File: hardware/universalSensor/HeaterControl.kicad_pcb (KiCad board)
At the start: 2 copper layers, 24.4 x 24.9 mm, 16 parts, among them J1 DS18B20, J4 Ext, P1 TC2030-CTX, SW1 BTN, U2 BL654, U3 SHT30-DIS-B

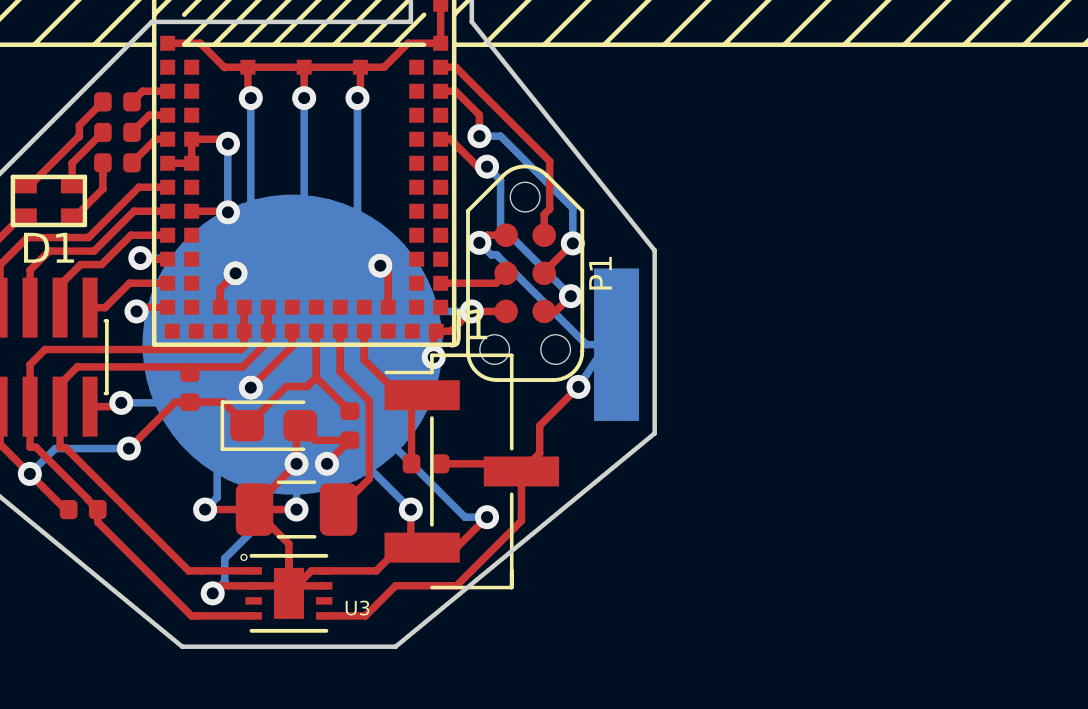
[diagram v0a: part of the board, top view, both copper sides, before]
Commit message: Add dev port do univeral board
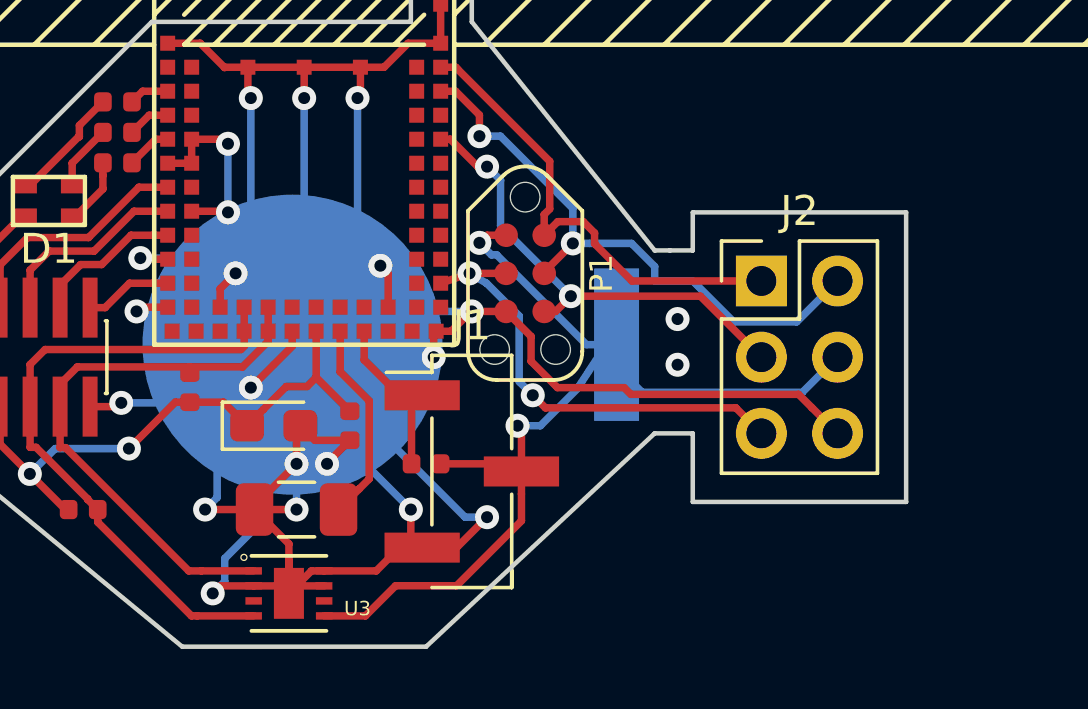
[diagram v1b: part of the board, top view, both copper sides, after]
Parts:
- added J2: DEV_PORT, Connector_PinHeader_2.54mm:PinHeader_2x03_P2.54mm_Vertical, F.Cu at (119.4, 86.4)
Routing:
- net GND: track 159.2 -> 172.5 mm
- net /nRESET: track 2.32 -> 15.4 mm, vias 0 -> 2
- net /SWDCLK_EXT: track 9.00 -> 19.8 mm
- net +3V3: track 50.3 -> 59.8 mm
- net /SWDIO_EXT: track 7.58 -> 16.8 mm, vias 0 -> 1
- net /SWO_EXT: track 8.50 -> 15.7 mm
- net (no net): vias 0 -> 2
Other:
- board size 24.4 x 24.9 mm -> 32.8 x 24.9 mm
